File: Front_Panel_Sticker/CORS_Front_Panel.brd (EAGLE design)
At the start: 156.6 x 39 mm, 18 parts

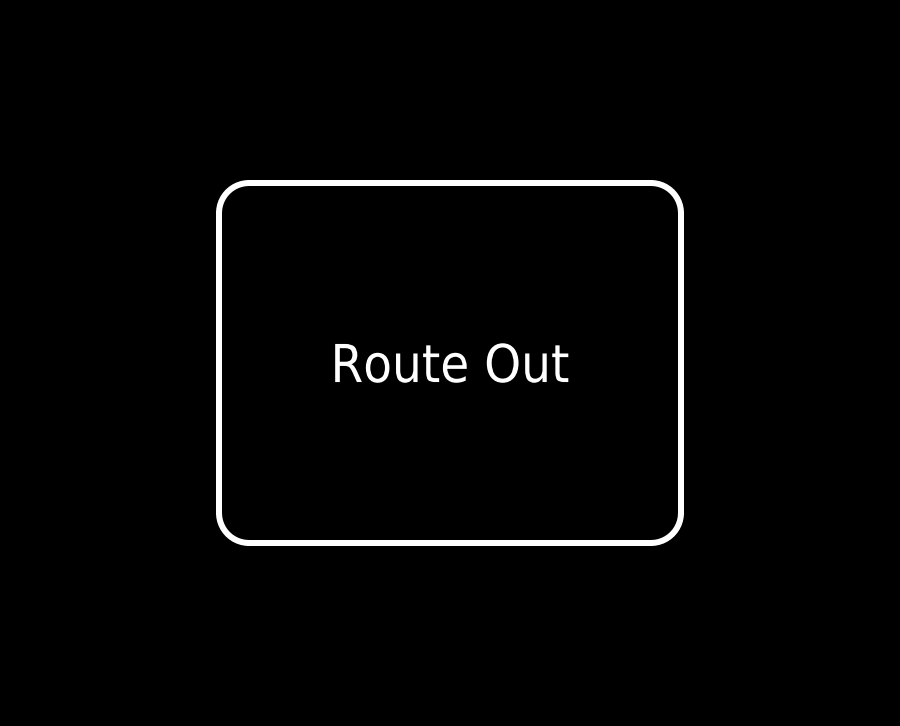
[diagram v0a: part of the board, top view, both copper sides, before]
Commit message: Update OLED and Ethernet
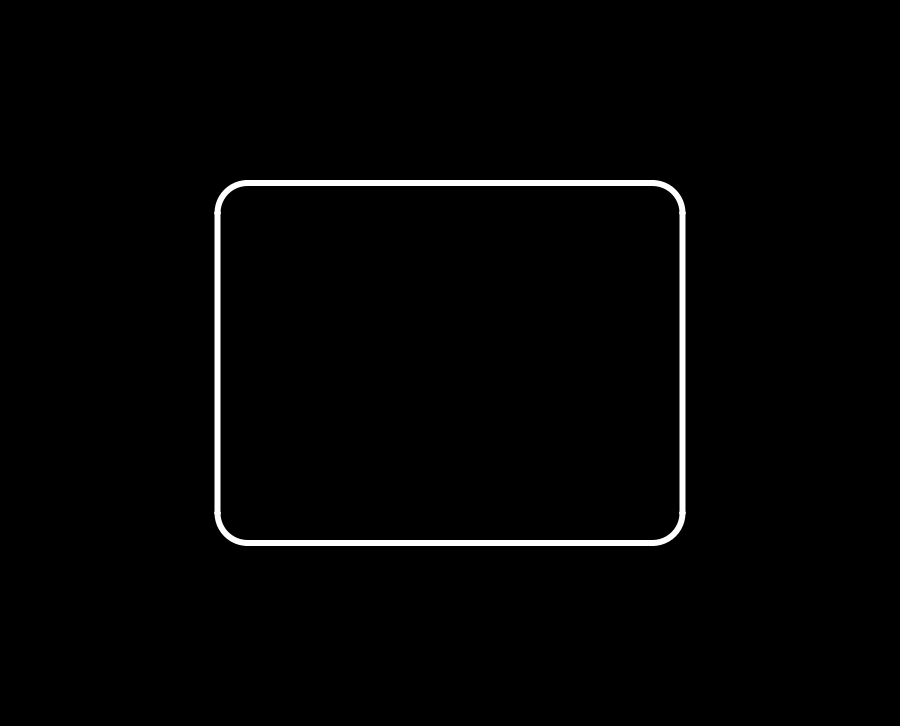
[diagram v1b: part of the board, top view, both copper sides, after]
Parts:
- removed OLED: OLED, CORS_Panels:OLED
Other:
- outline, holes or cut-outs redrawn
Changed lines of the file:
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@@
 <drawing>
 <settings>
-<setting alwaysvectorfont="yes"/>
+<setting alwaysvectorfont="no"/>
 <setting verticaltext="up"/>
 </settings>
@@
 <wire x1="-75.55" y1="0.75" x2="-78.3" y2="3.5" width="0.2" layer="20" curve="-90"/>
 <wire x1="-67.8" y1="-7" x2="-70.55" y2="-4.25" width="0.2" layer="20" curve="-90"/>
+<wire x1="-6.75" y1="18.5" x2="6.75" y2="18.5" width="0.2" layer="20"/>
+<wire x1="-6.75" y1="18.5" x2="-7.75" y2="17.5" width="0.2" layer="20" curve="90"/>
+<wire x1="-7.75" y1="17.5" x2="-7.75" y2="7.5" width="0.2" layer="20"/>
+<wire x1="7.75" y1="17.5" x2="7.75" y2="7.5" width="0.2" layer="20"/>
+<wire x1="7.75" y1="17.5" x2="6.75" y2="18.5" width="0.2" layer="20" curve="90"/>
+<wire x1="6.75" y1="6.5" x2="7.75" y2="7.5" width="0.2" layer="20" curve="90"/>
+<wire x1="-6.75" y1="6.5" x2="6.75" y2="6.5" width="0.2" layer="20"/>
+<wire x1="-7.75" y1="7.5" x2="-6.75" y2="6.5" width="0.2" layer="20" curve="90"/>
 </plain>
 <attributes>
@@
 <element name="ESP32_USB" library="CORS_Panels" package="USB-C" value="USB-C" x="38.1" y="0" smashed="yes"/>
 <element name="GNSS_USB" library="CORS_Panels" package="USB-C" value="USB-C" x="63.5" y="0" smashed="yes"/>
-<element name="OLED" library="CORS_Panels" package="OLED" value="OLED" x="0" y="12.5" smashed="yes"/>
 <element name="LOGO1" library="SparkFun-Aesthetics" package="SFE_LOGO_NAME_FLAME_.3" value="SFE_LOGO_NAME_FLAME.3_INCH" x="-46.8504" y="17.0889" smashed="yes"/>
 <element name="U$1" library="output" package="REFERENCE_STATION0" value="" x="44" y="18" smashed="yes"/>

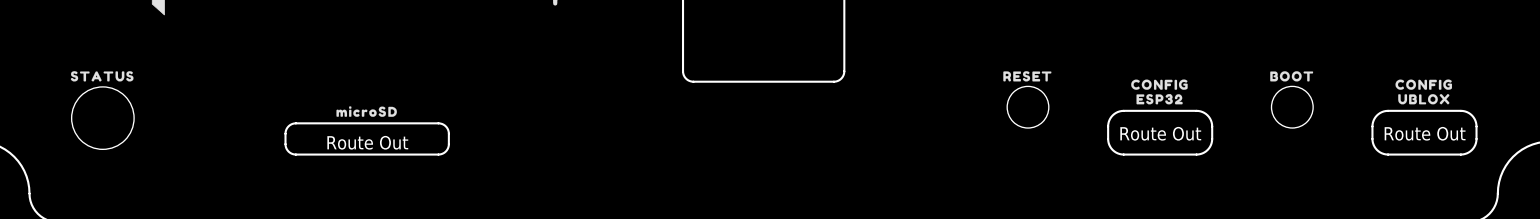
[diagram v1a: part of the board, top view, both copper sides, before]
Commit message: Update stickers
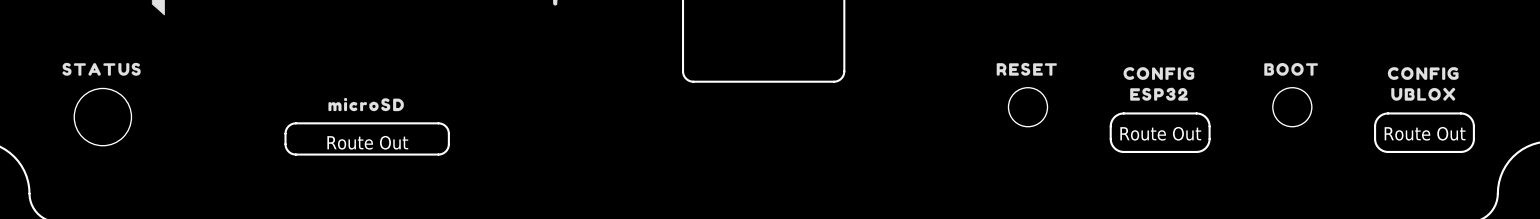
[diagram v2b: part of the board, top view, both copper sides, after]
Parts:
- removed MICROSD: (no value), output:MICROSD0
- removed RESET_LABEL: (no value), output:RESET0
- removed U$2: (no value), output:BOOT0
- removed U$3, U$4: (no value), output:CONFIG0
- removed U$5: (no value), output:ESP320
- removed U$6: (no value), output:UBLOX0
- added U$10, U$9: (no value), output:CONFIG3
- added U$11: (no value), output:ESP324
- added U$12: (no value), output:BOOT325
- added U$13: (no value), output:UBLOX326
- added U$7: (no value), output:MICROSD1
- added U$8: (no value), output:RESET2
- moved STATUS 0.67 mm to (-63.5, 7.67)
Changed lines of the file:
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@@
 <setting verticaltext="up"/>
 </settings>
-<grid distance="1" unitdist="mm" unit="mm" style="lines" multiple="1" display="yes" altdistance="0.1" altunitdist="mm" altunit="mm"/>
+<grid distance="0.05" unitdist="inch" unit="inch" style="lines" multiple="1" display="yes" altdistance="0.005" altunitdist="inch" altunit="inch"/>
 <layers>
 <layer number="1" name="Top" color="4" fill="1" visible="yes" active="yes"/>
@@
 <element name="LOGO1" library="SparkFun-Aesthetics" package="SFE_LOGO_NAME_FLAME_.3" value="SFE_LOGO_NAME_FLAME.3_INCH" x="-46.8504" y="17.0889" smashed="yes"/>
 <element name="U$1" library="output" package="REFERENCE_STATION0" value="" x="44" y="18" smashed="yes"/>
-<element name="STATUS" library="output" package="STATUS0" value="" x="-63.5" y="7" smashed="yes"/>
-<element name="MICROSD" library="output" package="MICROSD0" value="" x="-38.1" y="3.6" smashed="yes"/>
-<element name="RESET_LABEL" library="output" package="RESET0" value="" x="25.4" y="7" smashed="yes"/>
-<element name="U$2" library="output" package="BOOT0" value="" x="50.8" y="7" smashed="yes"/>
-<element name="U$3" library="output" package="CONFIG0" value="" x="38.1" y="6.2" smashed="yes"/>
-<element name="U$4" library="output" package="CONFIG0" value="" x="63.5" y="6.2" smashed="yes"/>
-<element name="U$5" library="output" package="ESP320" value="" x="38.1" y="4.8" smashed="yes"/>
-<element name="U$6" library="output" package="UBLOX0" value="" x="63.5" y="4.8" smashed="yes"/>
+<element name="STATUS" library="output" package="STATUS0" value="" x="-63.54" y="7.67" smashed="yes"/>
+<element name="U$7" library="output" package="MICROSD1" value="" x="-38.14" y="4.27" smashed="yes"/>
+<element name="U$8" library="output" package="RESET2" value="" x="25.36" y="7.67" smashed="yes"/>
+<element name="U$9" library="output" package="CONFIG3" value="" x="38.06" y="7.27" smashed="yes"/>
+<element name="U$10" library="output" package="CONFIG3" value="" x="63.46" y="7.27" smashed="yes"/>
+<element name="U$11" library="output" package="ESP324" value="" x="38.06" y="5.27" smashed="yes"/>
+<element name="U$12" library="output" package="BOOT325" value="" x="50.76" y="7.67" smashed="yes"/>
+<element name="U$13" library="output" package="UBLOX326" value="" x="63.46" y="5.27" smashed="yes"/>
 </elements>
 <signals>

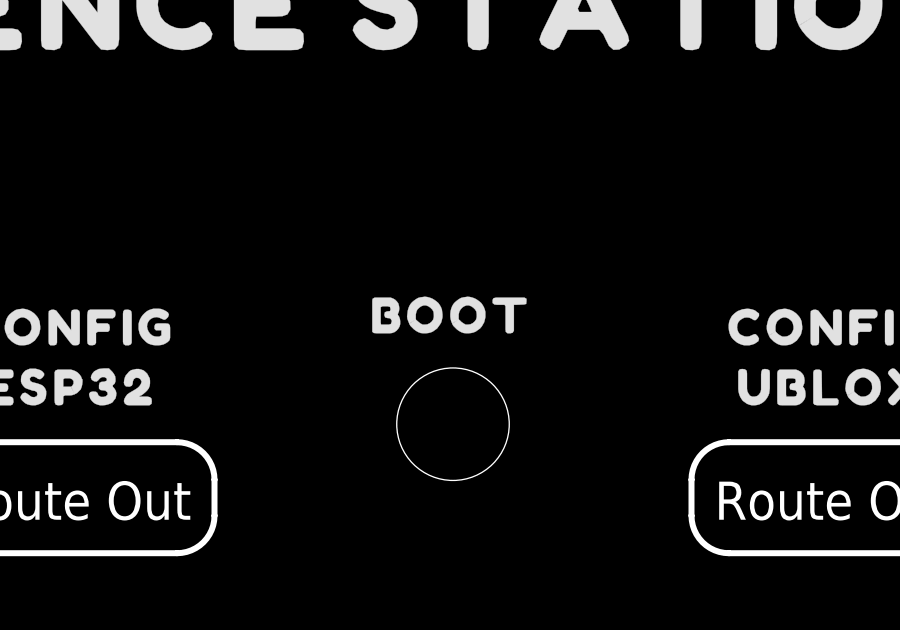
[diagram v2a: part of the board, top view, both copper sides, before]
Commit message: Move BOOT / MODE button further out. Update panels and stickers
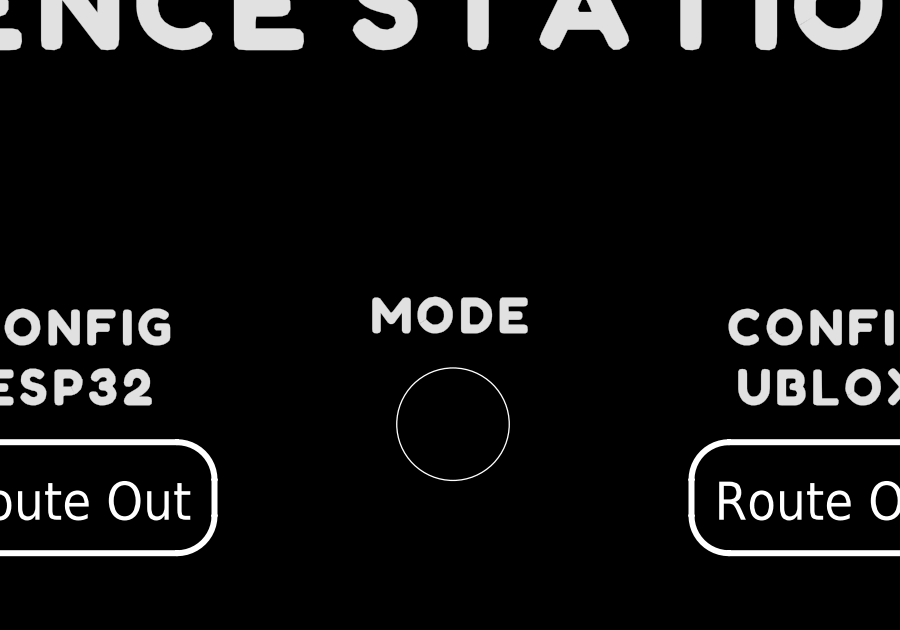
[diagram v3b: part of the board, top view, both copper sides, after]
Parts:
- removed U$12: (no value), output:BOOT325
- added U$2: (no value), output:MODE0
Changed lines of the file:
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@@
 <drawing>
 <settings>
-<setting alwaysvectorfont="no"/>
+<setting alwaysvectorfont="yes"/>
 <setting verticaltext="up"/>
 </settings>
-<grid distance="0.05" unitdist="inch" unit="inch" style="lines" multiple="1" display="yes" altdistance="0.005" altunitdist="inch" altunit="inch"/>
+<grid distance="1" unitdist="mm" unit="mm" style="lines" multiple="1" display="yes" altdistance="0.1" altunitdist="mm" altunit="mm"/>
 <layers>
 <layer number="1" name="Top" color="4" fill="1" visible="yes" active="yes"/>
@@
 <element name="U$10" library="output" package="CONFIG3" value="" x="63.46" y="7.27" smashed="yes"/>
 <element name="U$11" library="output" package="ESP324" value="" x="38.06" y="5.27" smashed="yes"/>
-<element name="U$12" library="output" package="BOOT325" value="" x="50.76" y="7.67" smashed="yes"/>
 <element name="U$13" library="output" package="UBLOX326" value="" x="63.46" y="5.27" smashed="yes"/>
+<element name="U$2" library="output" package="MODE0" value="" x="50.76" y="7.67" smashed="yes"/>
 </elements>
 <signals>
